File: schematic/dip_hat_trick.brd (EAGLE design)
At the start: 61.3 x 59.3 mm, 12 parts, among them IC2 DS2432P, X1 RPi

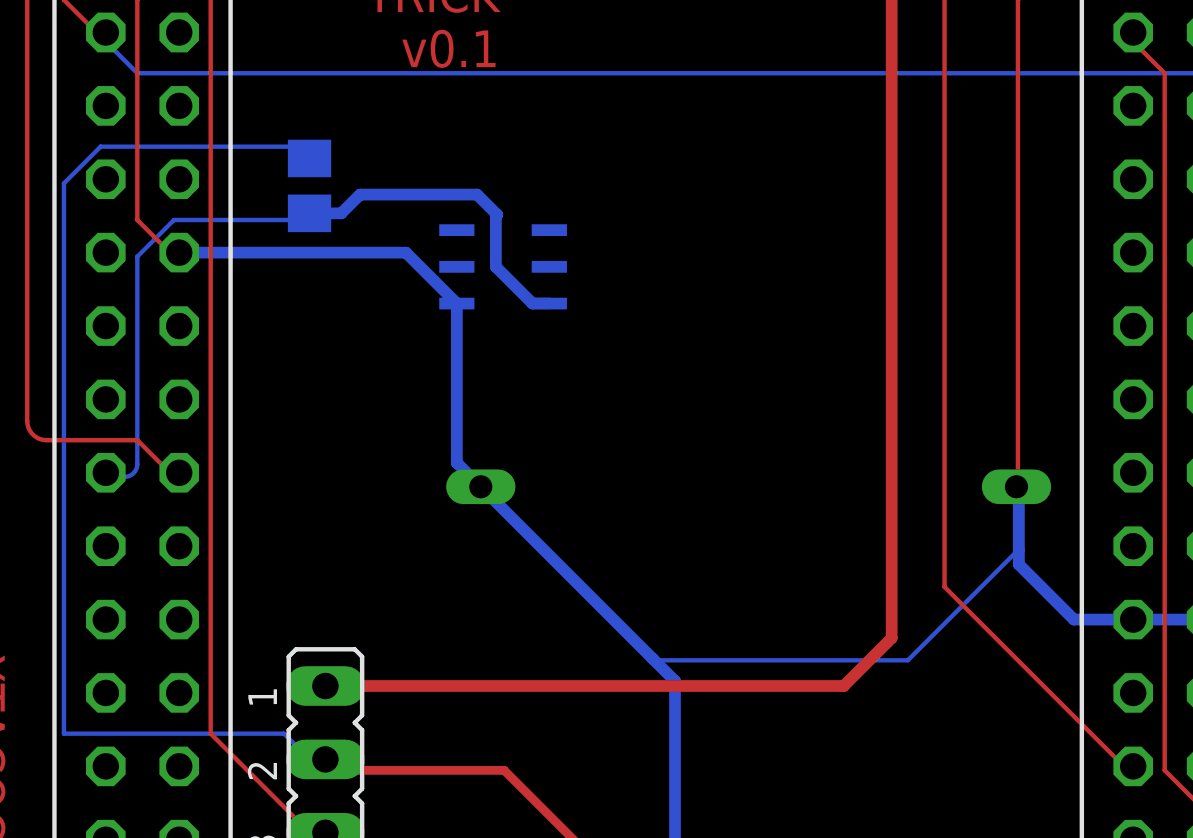
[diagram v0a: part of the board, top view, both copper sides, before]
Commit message: Update to the DS2431 per info from @KoljaWindeler, Adding pdfs of the Schematic and PCB
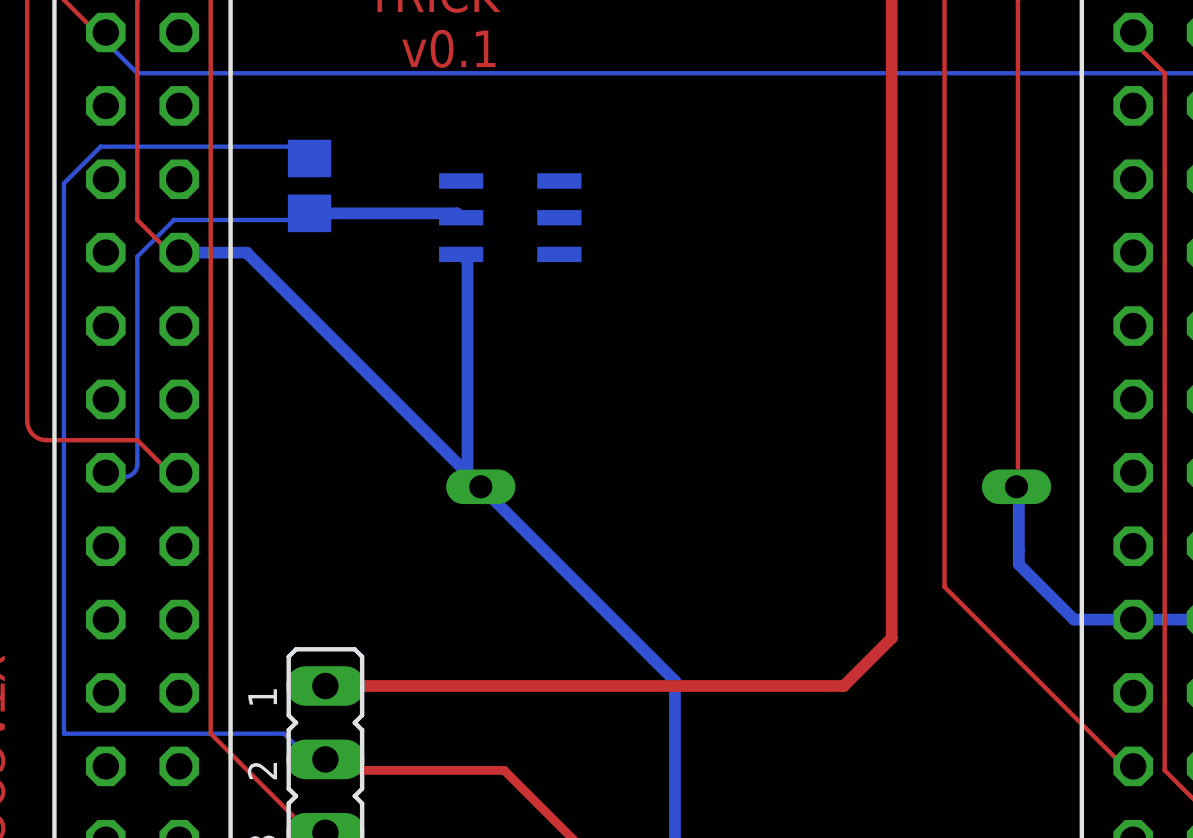
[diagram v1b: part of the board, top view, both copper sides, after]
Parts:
- removed IC2: DS2432P, 1wire:TSOC6
- added U1: DS2431P, JKW_CHIP:TSOC6
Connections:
- net GND: now also U1.1; no longer IC2.4
- net LCD-D2: now also U1.2; no longer IC2.3
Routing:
- net GND: track 189.9 -> 180.8 mm
- net LCD-D2: track 27.4 -> 21.5 mm
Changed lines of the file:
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@@
 <layer number="112" name="tSilk" color="7" fill="1" visible="yes" active="yes"/>
 <layer number="113" name="IDFDebug" color="7" fill="1" visible="yes" active="yes"/>
+<layer number="114" name="Badge_Outline" color="7" fill="1" visible="yes" active="yes"/>
+<layer number="115" name="ReferenceISLANDS" color="7" fill="1" visible="yes" active="yes"/>
 <layer number="116" name="Patch_BOT" color="9" fill="4" visible="yes" active="yes"/>
 <layer number="118" name="Rect_Pads" color="7" fill="1" visible="no" active="no"/>
@@
 <layer number="154" name="FabDoc2" color="7" fill="1" visible="yes" active="yes"/>
 <layer number="155" name="FabDoc3" color="7" fill="1" visible="yes" active="yes"/>
+<layer number="156" name="tAssmbl" color="7" fill="1" visible="yes" active="yes"/>
+<layer number="157" name="bAssmbl" color="7" fill="1" visible="yes" active="yes"/>
 <layer number="199" name="Contour" color="7" fill="1" visible="yes" active="yes"/>
 <layer number="200" name="200bmp" color="1" fill="10" visible="yes" active="yes"/>
@@
 <attribute name="VALUE" x="4.732" y="17.906" size="1.27" layer="27" ratio="10" rot="R270"/>
 </element>
-<element name="IC2" library="1wire" package="TSOC6" value="DS2432P" x="15.2" y="31.4" smashed="yes" rot="MR270">
-<attribute name="NAME" x="13.86" y="28.16" size="1.27" layer="26" rot="MR180"/>
-<attribute name="VALUE" x="19.01" y="33.94" size="1.27" layer="28" rot="MR270"/>
-</element>
 <element name="R1" library="rcl" package="R0805" value="" x="8.5" y="34.2" smashed="yes" rot="MR90">
 <attribute name="NAME" x="10.27" y="32.515" size="1.27" layer="26" rot="MR90"/>
@@
 <attribute name="OC_FARNELL" value="unknown" x="24.8" y="59.3" size="1.778" layer="27" display="off"/>
 </element>
+<element name="U1" library="JKW_CHIP" package="TSOC6" value="DS2431P" x="15.45" y="33.1" rot="MR90">
+<attribute name="ASSEMBLE" value="" x="15.45" y="33.1" size="1.778" layer="28" rot="MR90" display="off"/>
+<attribute name="PART_TYPE" value="IC" x="15.45" y="33.1" size="1.778" layer="28" rot="MR90" display="off"/>
+<attribute name="VENDOR_PART_NUMBER" value="DS2431P+T&amp;R" x="15.45" y="33.1" size="1.778" layer="28" rot="MR90" display="off"/>
+<attribute name="PRICE" value="0.98" x="15.45" y="33.1" size="1.778" layer="28" rot="MR90" display="off"/>
+<attribute name="TOLLERANCE" value="" x="15.45" y="33.1" size="1.778" layer="28" rot="MR90" display="off"/>
+<attribute name="DESCRIPTION" value="IC, 1024-Bit, 1-Wire EEPROM, TSOC6" x="15.45" y="33.1" size="1.778" layer="28" rot="MR90" display="off"/>
+<attribute name="FOOTPRINT" value="TSOC6" x="15.45" y="33.1" size="1.778" layer="28" rot="MR90" display="off"/>
+<attribute name="MFG" value="DIGIKEY" x="15.45" y="33.1" size="1.778" layer="28" rot="MR90" display="off"/>
+<attribute name="VENDOR" value="MAXIM" x="15.45" y="33.1" size="1.778" layer="28" rot="MR90" display="off"/>
+<attribute name="LINK" value="http://www.digikey.com/product-detail/en/DS2431P%2BT%26R/DS2431P%2BT%26RCT-ND/3647900" x="15.45" y="33.1" size="1.778" layer="28" rot="MR90" display="off"/>
+<attribute name="MFG_PN" value="DS2431P+T&amp;RCT-ND" x="15.45" y="33.1" size="1.778" layer="28" rot="MR90" display="off"/>
+</element>
 </elements>
 <signals>
@@
 <contactref element="U$9" pad="GNDIN"/>
 <contactref element="U$9" pad="GNDOUT"/>
-<contactref element="IC2" pad="4"/>
-<contactref element="IC2" pad="4"/>
 <wire x1="3.99" y1="42.05" x2="4.11" y2="42.17" width="0.4064" layer="1"/>
 <contactref element="GND5" pad="1"/>
@@
 <wire x1="21.15" y1="3.25" x2="21.15" y2="17.064" width="0.4064" layer="16"/>
 <wire x1="21.15" y1="17.064" x2="20.377" y2="17.837" width="0.4064" layer="16"/>
-<wire x1="20.377" y1="17.837" x2="14.428" y2="23.786" width="0.4064" layer="16"/>
 <wire x1="39.55" y1="19.19" x2="37.01" y2="19.19" width="0.4064" layer="16"/>
 <wire x1="37.01" y1="19.19" x2="34.96" y2="19.19" width="0.4064" layer="16"/>
@@
 <wire x1="33.05" y1="21.59" x2="33.05" y2="23.706" width="0.4064" layer="16"/>
 <wire x1="33.05" y1="23.706" x2="32.97" y2="23.786" width="0.4064" layer="16"/>
-<wire x1="13.5998" y1="30.13" x2="13.5998" y2="24.6142" width="0.4064" layer="16"/>
-<wire x1="13.5998" y1="24.6142" x2="14.428" y2="23.786" width="0.4064" layer="16"/>
-<wire x1="3.99" y1="31.89" x2="11.8398" y2="31.89" width="0.4064" layer="16"/>
-<wire x1="11.8398" y1="31.89" x2="13.5998" y2="30.13" width="0.4064" layer="16"/>
 <wire x1="37.01" y1="44.59" x2="37.01" y2="45.17" width="0.4064" layer="16"/>
 <wire x1="37.01" y1="45.17" x2="31.15" y2="51.03" width="0.4064" layer="16"/>
@@
 <wire x1="3.81" y1="41.91" x2="3.99" y2="42.05" width="0.1524" layer="1"/>
 <wire x1="3.81" y1="31.75" x2="3.99" y2="31.89" width="0.1524" layer="1"/>
-<wire x1="29.21" y1="17.78" x2="33.02" y2="21.59" width="0.1524" layer="16"/>
-<wire x1="20.32" y1="17.78" x2="29.21" y2="17.78" width="0.1524" layer="16"/>
 <wire x1="33.02" y1="21.59" x2="33.05" y2="21.59" width="0.1524" layer="16"/>
 <wire x1="20.32" y1="17.78" x2="20.377" y2="17.837" width="0.1524" layer="16"/>
@@
 <wire x1="36.83" y1="44.45" x2="37.01" y2="44.59" width="0.1524" layer="1"/>
 <wire x1="33.02" y1="24.13" x2="32.97" y2="23.786" width="0.1524" layer="1"/>
+<wire x1="13.97" y1="24.13" x2="14.428" y2="23.786" width="0.1524" layer="16"/>
+<wire x1="3.99" y1="31.89" x2="6.324" y2="31.89" width="0.4064" layer="16"/>
+<wire x1="6.324" y1="31.89" x2="14.428" y2="23.786" width="0.4064" layer="16"/>
+<wire x1="14.428" y1="23.786" x2="20.377" y2="17.837" width="0.4064" layer="16"/>
+<contactref element="U1" pad="1"/>
+<wire x1="1.45" y1="44.59" x2="5.75" y2="53.57" width="0" layer="19" extent="1-1"/>
+<wire x1="13.97" y1="24.13" x2="13.97" y2="31.6098" width="0.4064" layer="16"/>
+<wire x1="13.97" y1="31.6098" x2="13.7498" y2="31.83" width="0.4064" layer="16"/>
 </signal>
 <signal name="XIO-P5">
@@
 <signal name="LCD-D2">
 <contactref element="SV2" pad="19"/>
-<contactref element="IC2" pad="3"/>
 <contactref element="R1" pad="1"/>
 <wire x1="3.81" y1="33.02" x2="8.89" y2="33.02" width="0.1524" layer="16"/>
@@
 <wire x1="8.89" y1="33.02" x2="8.5" y2="33.25" width="0.1524" layer="16"/>
 <wire x1="1.27" y1="24.13" x2="1.45" y2="24.27" width="0.1524" layer="16"/>
-<wire x1="16.8002" y1="30.13" x2="16.22" y2="30.13" width="0.4064" layer="16"/>
-<wire x1="16.22" y1="30.13" x2="14.95" y2="31.4" width="0.4064" layer="16"/>
-<wire x1="14.95" y1="31.4" x2="14.95" y2="33.15" width="0.4064" layer="16"/>
-<wire x1="14.95" y1="33.15" x2="15" y2="33.2" width="0.4064" layer="16"/>
-<wire x1="15" y1="33.2" x2="14.3" y2="33.9" width="0.4064" layer="16"/>
-<wire x1="14.3" y1="33.9" x2="10.25" y2="33.9" width="0.4064" layer="16"/>
-<wire x1="10.25" y1="33.9" x2="9.6" y2="33.25" width="0.4064" layer="16"/>
-<wire x1="9.6" y1="33.25" x2="8.5" y2="33.25" width="0.4064" layer="16"/>
+<contactref element="U1" pad="2"/>
+<wire x1="8.5" y1="33.25" x2="13.5998" y2="33.25" width="0.4064" layer="16"/>
+<wire x1="13.5998" y1="33.25" x2="13.7498" y2="33.1" width="0.4064" layer="16"/>
 </signal>
 </signals>
